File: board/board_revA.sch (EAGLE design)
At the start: 64 parts, among them Q2 ULN2003AD, Y1 8Mhz 20pF

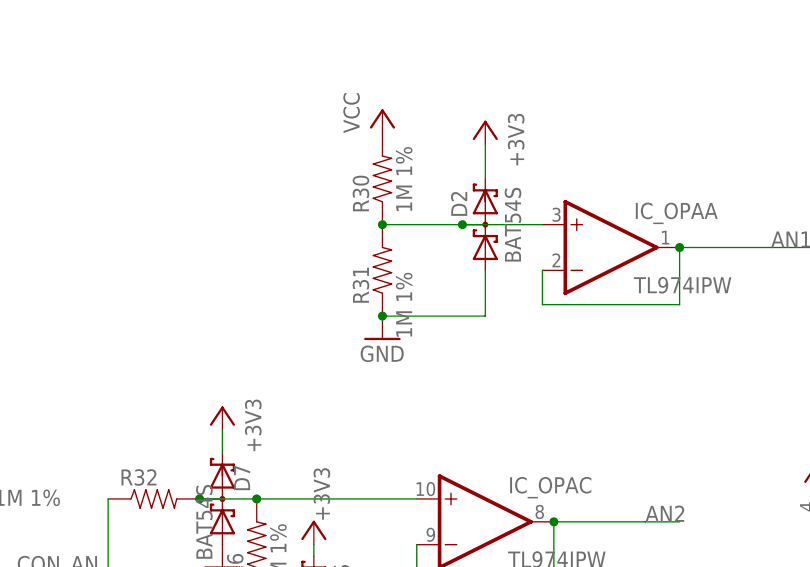
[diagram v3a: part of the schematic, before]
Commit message: [Board A] Fixed resistor values
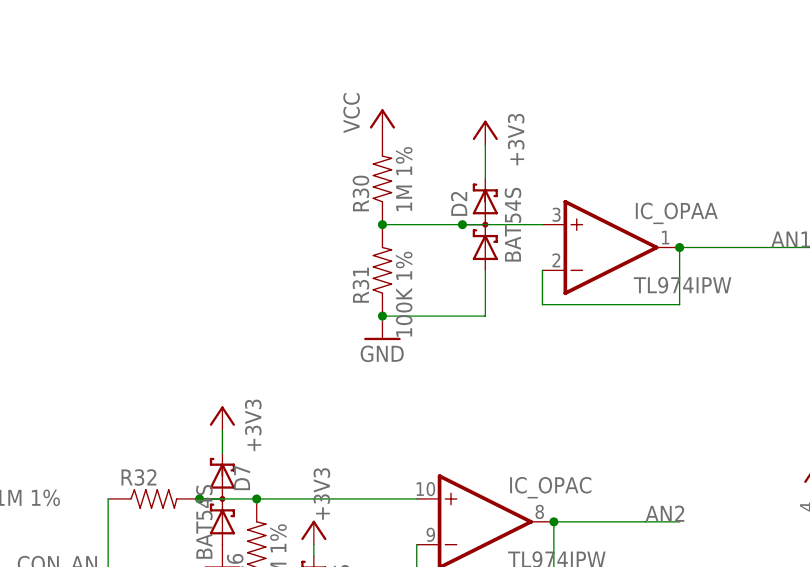
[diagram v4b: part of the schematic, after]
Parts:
- R31: value 1M 1% -> 100K 1%
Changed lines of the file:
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@@
 <setting verticaltext="up"/>
 </settings>
-<grid distance="0.1" unitdist="inch" unit="inch" style="lines" multiple="1" display="no" altdistance="0.01" altunitdist="inch" altunit="inch"/>
+<grid distance="0.05" unitdist="inch" unit="inch" style="lines" multiple="1" display="yes" altdistance="0.005" altunitdist="inch" altunit="inch"/>
 <layers>
 <layer number="1" name="Top" color="4" fill="1" visible="no" active="no"/>
@@
 <part name="GND35" library="supply1" deviceset="GND" device=""/>
 <part name="R30" library="SparkFun-Resistors" deviceset="RESISTOR" device="0603-RES" value="1M 1%"/>
-<part name="R31" library="SparkFun-Resistors" deviceset="RESISTOR" device="0603-RES" value="1M 1%"/>
+<part name="R31" library="SparkFun-Resistors" deviceset="RESISTOR" device="0603-RES" value="100K 1%"/>
 <part name="GND34" library="supply1" deviceset="GND" device=""/>
 <part name="P+10" library="supply1" deviceset="VCC" device=""/>
